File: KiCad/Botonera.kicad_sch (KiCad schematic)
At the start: 0 parts

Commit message: he canviat el micro
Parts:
- added R10, R11, R12, R7, R8, R9: 10K, symbol Device:R
- added SW1, SW2, SW3, SW4, SW5, SW6: SW_Push, symbol Switch:SW_Push
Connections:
- new net 3V3: R10.1, R11.1, R12.1, R7.1, R8.1, R9.1
- new net CARRETERA: R7.2, SW1.1
- new net DIURNA: R9.2, SW3.1
- new net ENCREUAMENT: R8.2, SW2.1
- new net GND: SW1.2, SW2.2, SW3.2, SW4.2, SW5.2, SW6.2
- new net INTERM. DRT: R11.2, SW5.1
- new net INTERM. ESQ: R12.2, SW6.1
- new net NETEJA-FARS: R10.2, SW4.1
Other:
- note added: "BOTONERA"

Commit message: ERC i footprints
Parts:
- R10, R11, R12, R7, R8, R9: footprint (none) -> Resistor_SMD:R_0805_2012Metric_Pad1.20x1.40mm_HandSolder
- SW1, SW2, SW3, SW4, SW5, SW6: footprint (none) -> Button_Switch_THT:SW_PUSH_6mm
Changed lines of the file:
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@@
 	(text "BOTONERA"
 		(exclude_from_sim no)
-		(at 146.812 72.898 0)
+		(at 146.812 68.834 0)
 		(effects
 			(font
@@
 			)
 		)
-		(property "Footprint" ""
+		(property "Footprint" "Button_Switch_THT:SW_PUSH_6mm"
 			(at 180.34 81.28 0)
 			(effects
@@
 			)
 		)
-		(property "Footprint" ""
+		(property "Footprint" "Button_Switch_THT:SW_PUSH_6mm"
 			(at 127 96.52 0)
 			(effects
@@
 			)
 		)
-		(property "Footprint" ""
+		(property "Footprint" "Button_Switch_THT:SW_PUSH_6mm"
 			(at 127 111.76 0)
 			(effects
@@
 			)
 		)
-		(property "Footprint" ""
+		(property "Footprint" "Button_Switch_THT:SW_PUSH_6mm"
 			(at 180.34 111.76 0)
 			(effects
@@
 			)
 		)
-		(property "Footprint" ""
+		(property "Footprint" "Resistor_SMD:R_0805_2012Metric_Pad1.20x1.40mm_HandSolder"
 			(at 110.49 88.138 90)
 			(effects
@@
 			)
 		)
-		(property "Footprint" ""
+		(property "Footprint" "Resistor_SMD:R_0805_2012Metric_Pad1.20x1.40mm_HandSolder"
 			(at 110.49 103.378 90)
 			(effects
@@
 			)
 		)
-		(property "Footprint" ""
+		(property "Footprint" "Resistor_SMD:R_0805_2012Metric_Pad1.20x1.40mm_HandSolder"
 			(at 110.49 118.618 90)
 			(effects
@@
 			)
 		)
-		(property "Footprint" ""
+		(property "Footprint" "Resistor_SMD:R_0805_2012Metric_Pad1.20x1.40mm_HandSolder"
 			(at 163.83 88.138 90)
 			(effects
@@
 			)
 		)
-		(property "Footprint" ""
+		(property "Footprint" "Resistor_SMD:R_0805_2012Metric_Pad1.20x1.40mm_HandSolder"
 			(at 163.83 103.378 90)
 			(effects
@@
 			)
 		)
-		(property "Footprint" ""
+		(property "Footprint" "Button_Switch_THT:SW_PUSH_6mm"
 			(at 127 81.28 0)
 			(effects
@@
 			)
 		)
-		(property "Footprint" ""
+		(property "Footprint" "Button_Switch_THT:SW_PUSH_6mm"
 			(at 180.34 96.52 0)
 			(effects
@@
 			)
 		)
-		(property "Footprint" ""
+		(property "Footprint" "Resistor_SMD:R_0805_2012Metric_Pad1.20x1.40mm_HandSolder"
 			(at 163.83 118.618 90)
 			(effects

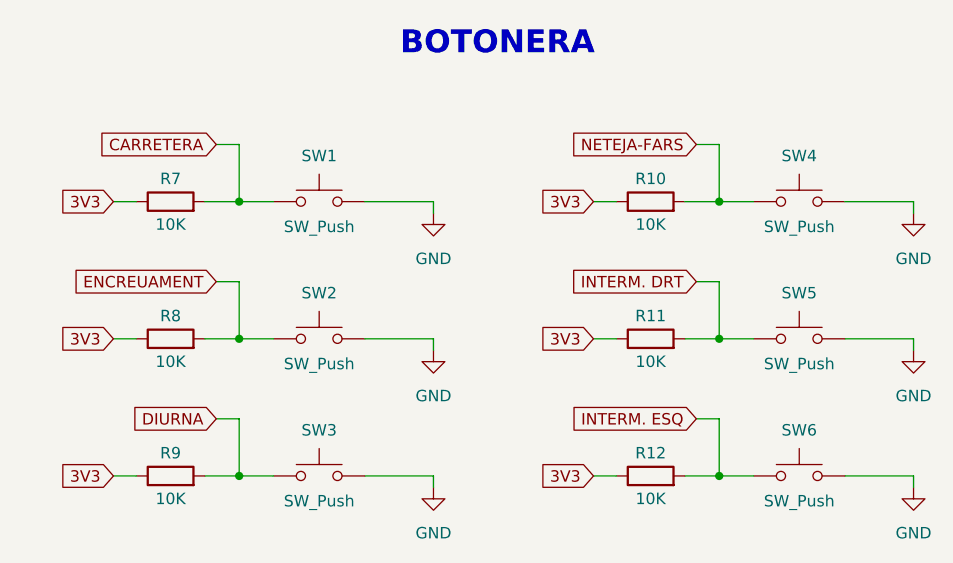
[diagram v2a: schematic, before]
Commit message: alguns errors de CADLAB i he canivat d'ordre els LEDs i els drivers a la PCB.
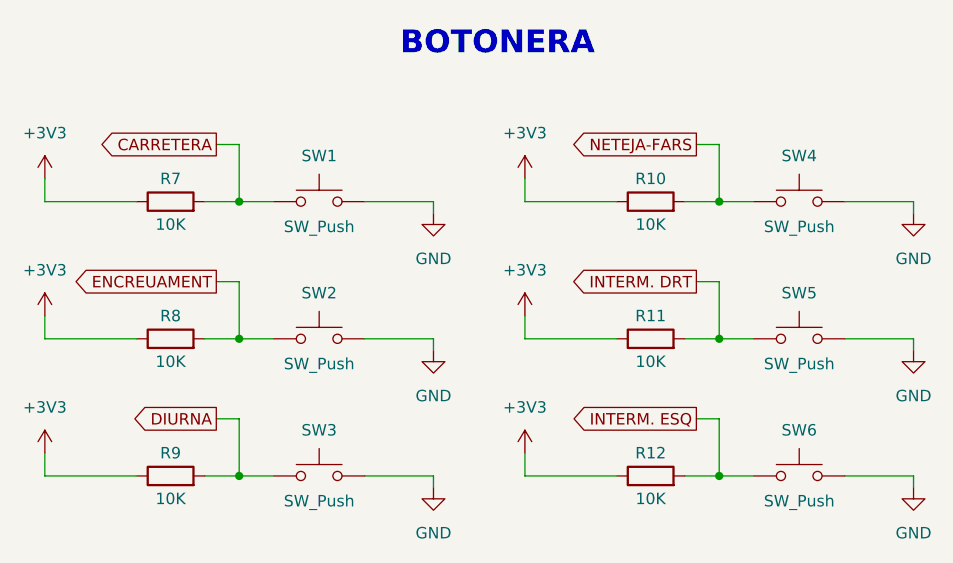
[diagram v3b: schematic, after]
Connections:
- net 3V3 renamed +3V3
